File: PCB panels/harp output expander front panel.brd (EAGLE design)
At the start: 133 x 35 mm, 1 part

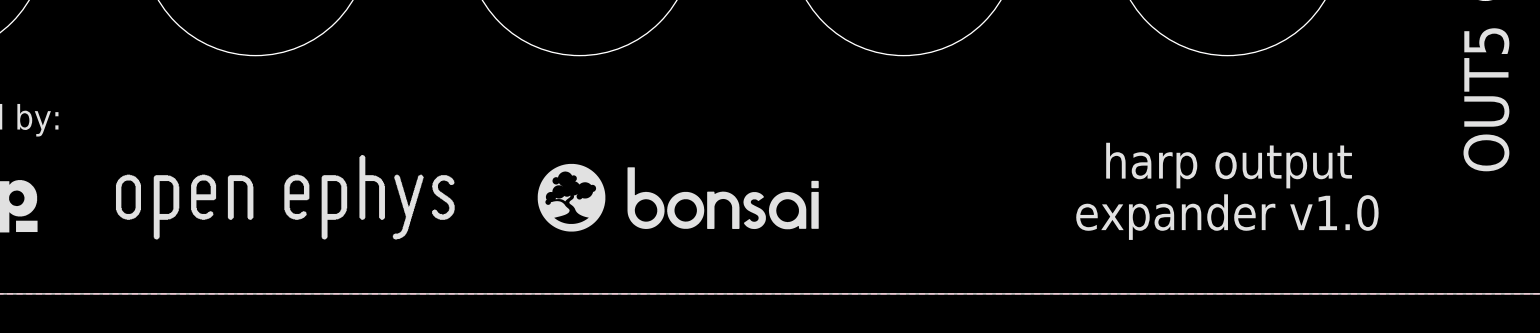
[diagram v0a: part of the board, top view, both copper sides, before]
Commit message: Updated panels to match PCB version.
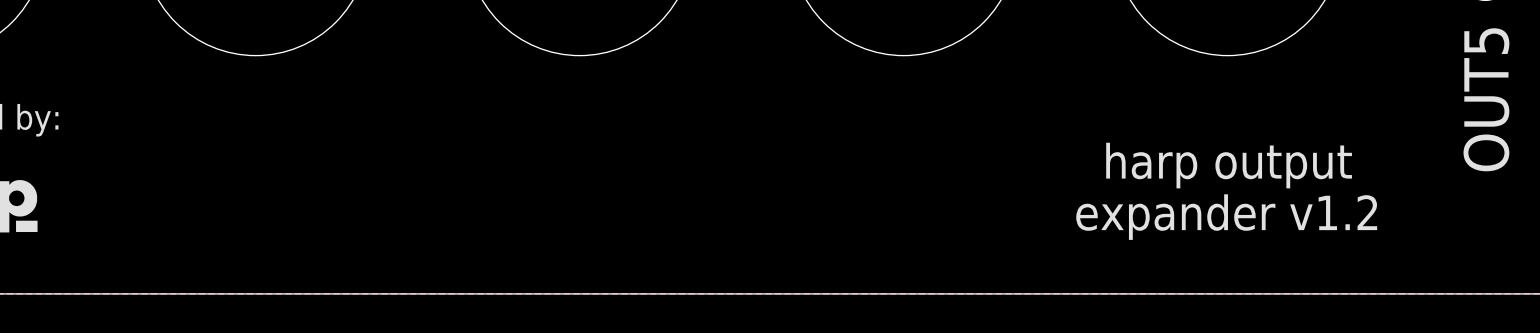
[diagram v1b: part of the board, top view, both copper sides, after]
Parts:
- removed U$30: OPEN_EPHYS_LOGO, open-ephys:OPEN_EPHYS_LOGO
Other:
- board text added: "harp output expander v1.2"
- board text removed: "harp output expander v1.0"
